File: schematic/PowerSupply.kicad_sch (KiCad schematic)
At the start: 0 parts

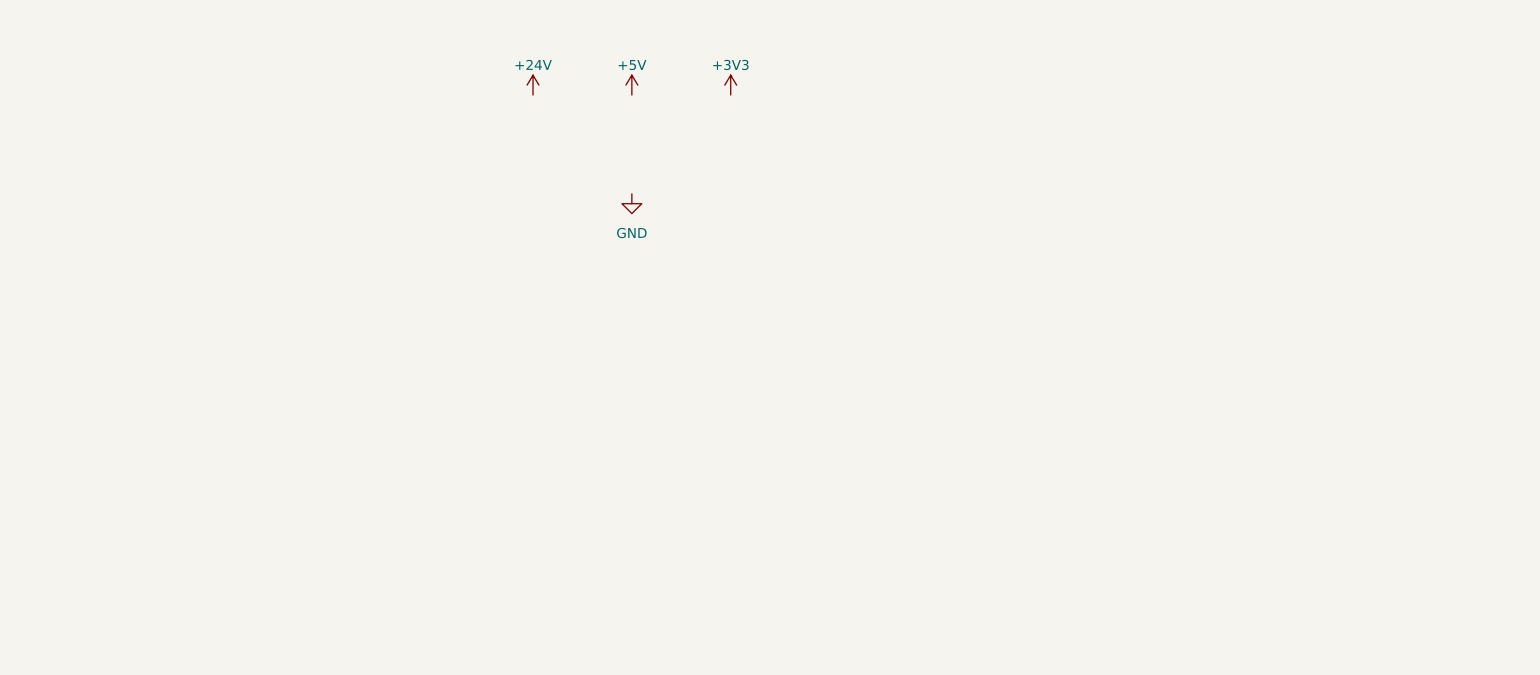
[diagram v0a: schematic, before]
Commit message: Create power supply schematic
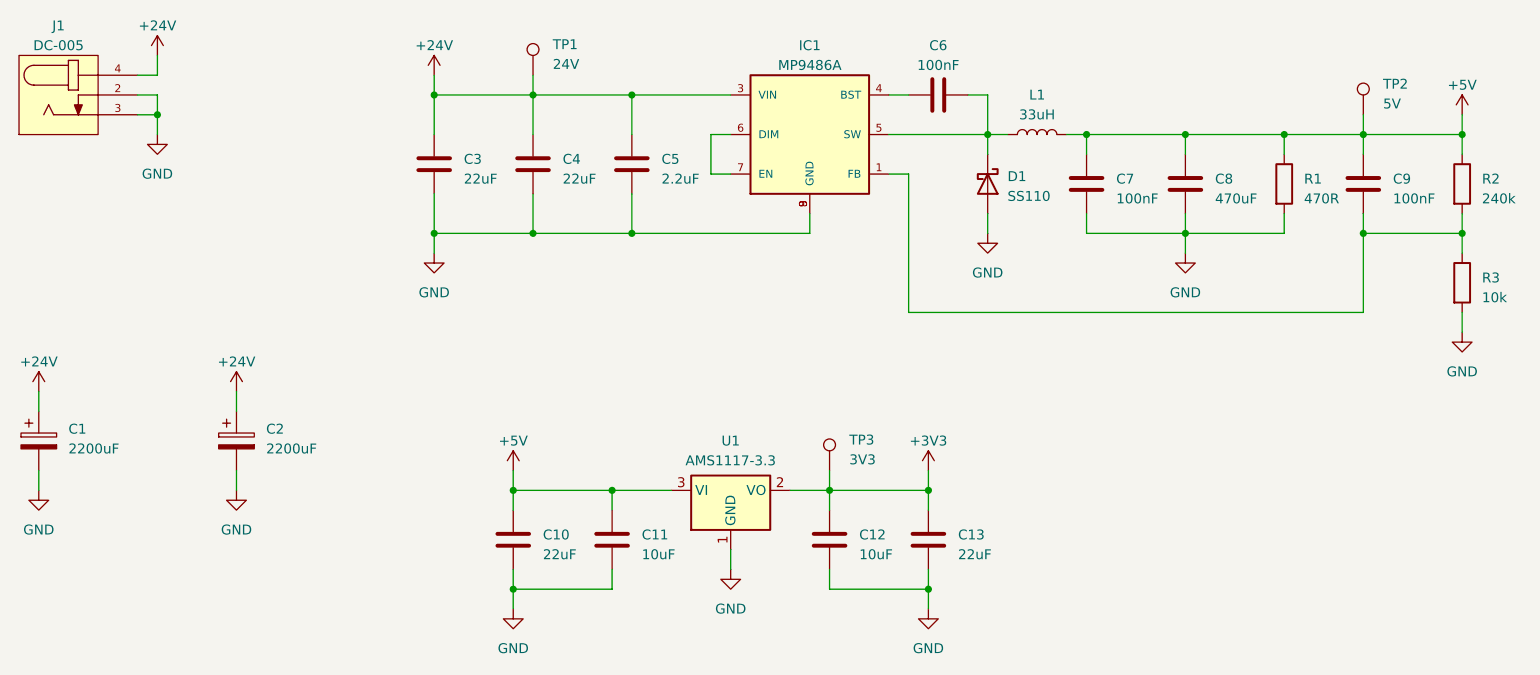
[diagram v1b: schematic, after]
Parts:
- added C1, C2: 2200uF, symbol Device:C_Polarized
- added C10, C13, C3, C4: 22uF, symbol Device:C
- added C11, C12: 10uF, symbol Device:C
- added C5: 2.2uF, symbol Device:C
- added C6, C7, C9: 100nF, symbol Device:C
- added C8: 470uF, symbol Device:C
- added D1: SS110, symbol Device:D_Schottky
- added IC1: MP9486A, MP9486A:SOIC-8EP, symbol MP9486A:MP9486A
- added J1: DC-005, DC-005:NINIGI_DC-005, symbol DC-005:DC-005
- added L1: 33uH, symbol Device:L
- added R1: 470R, symbol Device:R
- added R2: 240k, symbol Device:R
- added R3: 10k, symbol Device:R
- added TP1: 24V, symbol Connector:TestPoint
- added TP2: 5V, symbol Connector:TestPoint
- added TP3: 3V3, symbol Connector:TestPoint
- added U1: AMS1117-3.3, Package_TO_SOT_SMD:SOT-223-3_TabPin2, symbol Regulator_Linear:AMS1117-3.3
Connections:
- net +24V: now also C1.1, C2.1, C3.1, C4.1, C5.1, IC1.3 (VIN), J1.4, TP1.1
- net +3V3: now also C12.1, C13.1, TP3.1, U1.2 (VO)
- net +5V: now also C10.1, C11.1, C7.1, C8.1, C9.1, L1.2, R1.1, R2.1, TP2.1, U1.3 (VI)
- net GND: now also C1.2, C10.2, C11.2, C12.2, C13.2, C2.2, C3.2, C4.2, C5.2, C7.2, C8.2, D1.2 (A), IC1.8 (GND), IC1.9 (GND), J1.2, J1.3, R1.2, R3.2, U1.1 (GND)
- new net: C6.2, D1.1 (K), IC1.5 (SW), L1.1
- new net: C9.2, IC1.1 (FB), R2.2, R3.1
- new net: C6.1, IC1.4 (BST)
- new net: IC1.6 (DIM), IC1.7 (EN)

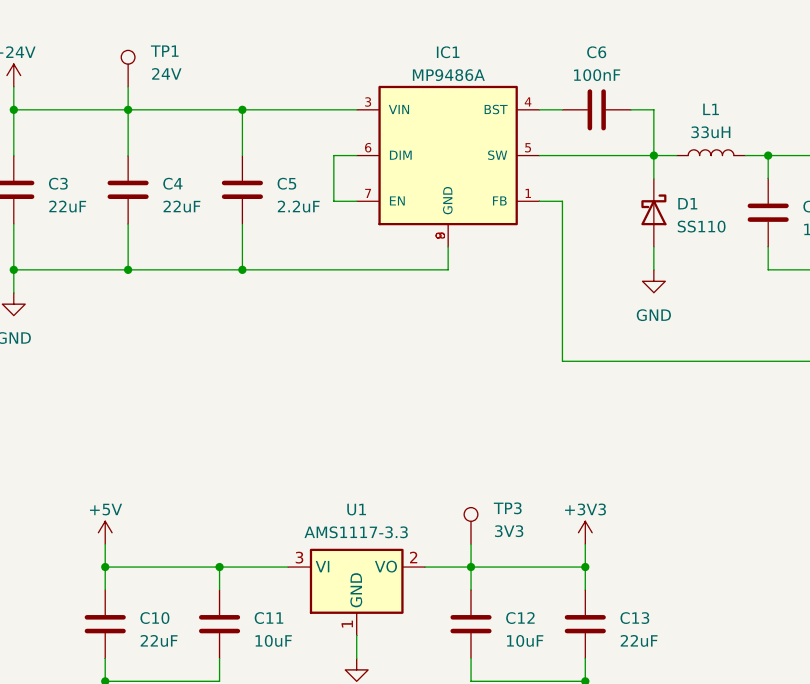
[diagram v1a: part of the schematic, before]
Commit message: Add test points to driver signals
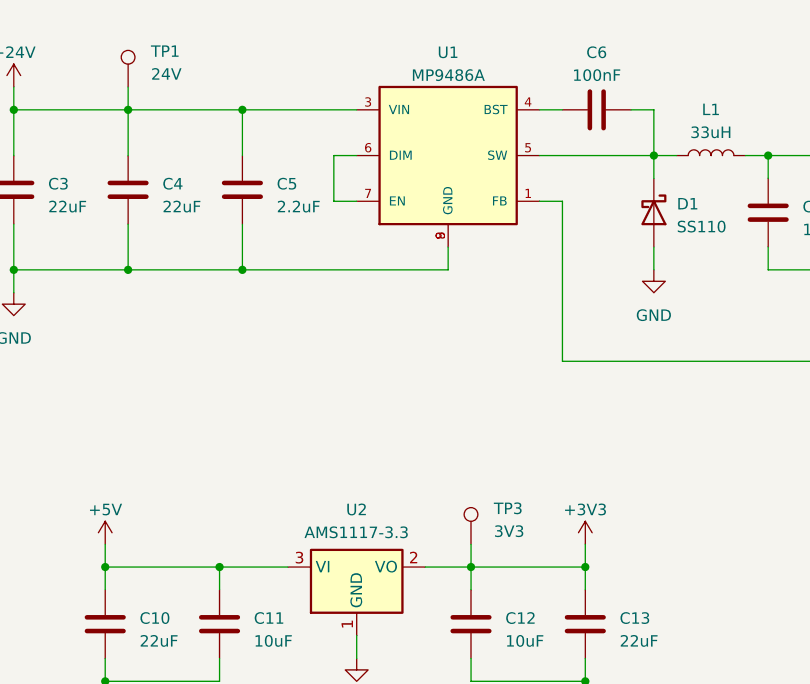
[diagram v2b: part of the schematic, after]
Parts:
- renumbered IC1 to U1, U1 to U2
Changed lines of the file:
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@@
   (symbol (lib_id "Regulator_Linear:AMS1117-3.3") (at 152.4 127 0) (unit 1)
     (in_bom yes) (on_board yes) (dnp no) (fields_autoplaced)
-    (property "Reference" "U1" (at 152.4 120.65 0)
+    (property "Reference" "U2" (at 152.4 120.65 0)
       (effects (font (size 1.27 1.27)))
     )
@@
       (project "uTesla"
         (path "/0cecab2b-a552-4f9c-b012-66fc2b7d8bdb/40e0481b-1d5b-49c7-bf9f-abcc1f3a7809"
-          (reference "U1") (unit 1)
+          (reference "U2") (unit 1)
         )
       )
@@
   (symbol (lib_id "MP9486A:MP9486A") (at 162.56 81.28 0) (unit 1)
     (in_bom yes) (on_board yes) (dnp no) (fields_autoplaced)
-    (property "Reference" "IC1" (at 162.56 69.85 0)
+    (property "Reference" "U1" (at 162.56 69.85 0)
       (effects (font (size 1.27 1.27)))
     )
@@
       (project "uTesla"
         (path "/0cecab2b-a552-4f9c-b012-66fc2b7d8bdb/40e0481b-1d5b-49c7-bf9f-abcc1f3a7809"
-          (reference "IC1") (unit 1)
-        )
-      )
+          (reference "U1") (unit 1)
+        )
+      )

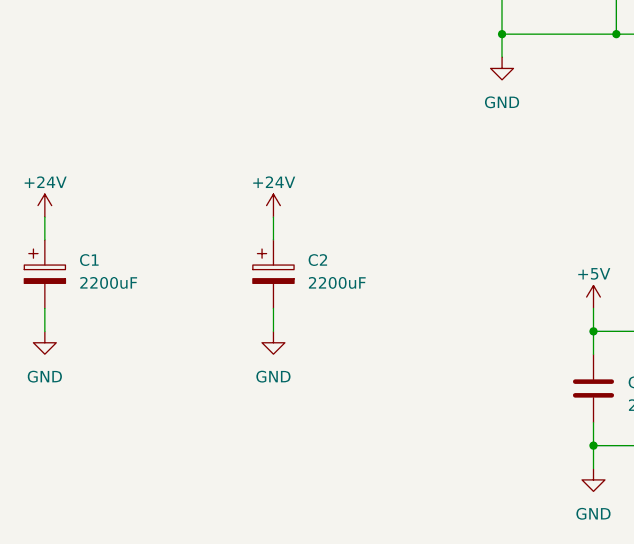
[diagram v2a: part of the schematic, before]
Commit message: Decrease input decoupling capacitance
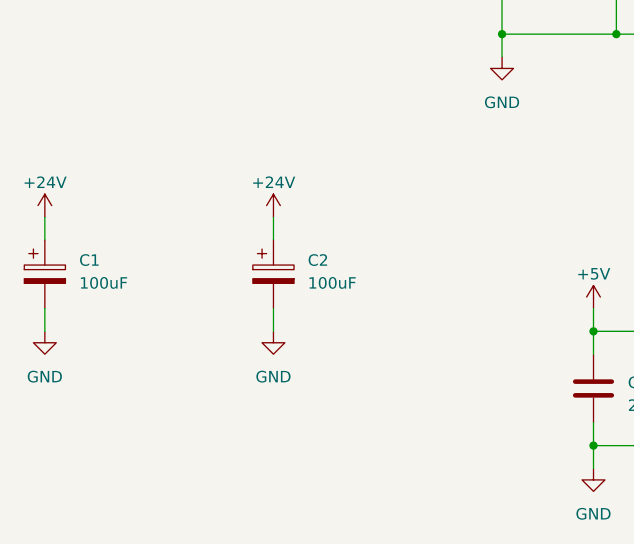
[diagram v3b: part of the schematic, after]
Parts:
- C1, C2: value 2200uF -> 100uF
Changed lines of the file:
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@@
       (effects (font (size 1.27 1.27)) (justify left))
     )
-    (property "Value" "2200uF" (at 92.71 121.666 0)
+    (property "Value" "100uF" (at 92.71 121.666 0)
       (effects (font (size 1.27 1.27)) (justify left))
     )
@@
       (effects (font (size 1.27 1.27)) (justify left))
     )
-    (property "Value" "2200uF" (at 67.31 121.666 0)
-      (effects (font (size 1.27 1.27)) (justify left))
-    )
+    (property "Value" "100uF" (at 67.31 121.666 0)
+      (effects (font (size 1.27 1.27)) (justify left))
+    )

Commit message: Assign footprints
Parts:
- C1, C2: footprint (none) -> Capacitor_THT:CP_Radial_D8.0mm_P3.80mm
- C10, C11, C12, C13, C3, C4, C5, C6, C7, C8, C9: footprint (none) -> Capacitor_SMD:C_0603_1608Metric
- D1: footprint (none) -> Diode_SMD:D_SMA
- L1: footprint (none) -> Inductor_THT:L_Toroid_Vertical_L26.7mm_W14.0mm_P10.16mm_Pulse_D
- R1, R2, R3: footprint (none) -> Resistor_SMD:R_0603_1608Metric
- TP1, TP2, TP3: footprint (none) -> TestPoint:TestPoint_Pad_D2.0mm
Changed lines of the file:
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@@
       (effects (font (size 1.27 1.27)) (justify left))
     )
-    (property "Footprint" "" (at 185.42 87.63 0)
+    (property "Footprint" "Diode_SMD:D_SMA" (at 185.42 87.63 0)
       (effects (font (size 1.27 1.27)) hide)
     )
@@
       (effects (font (size 1.27 1.27)) (justify left))
     )
-    (property "Footprint" "" (at 199.0852 91.44 0)
+    (property "Footprint" "Capacitor_SMD:C_0603_1608Metric" (at 199.0852 91.44 0)
       (effects (font (size 1.27 1.27)) hide)
     )
@@
       (effects (font (size 1.27 1.27)) (justify left))
     )
-    (property "Footprint" "" (at 127.9652 88.9 0)
+    (property "Footprint" "Capacitor_SMD:C_0603_1608Metric" (at 127.9652 88.9 0)
       (effects (font (size 1.27 1.27)) hide)
     )
@@
       (effects (font (size 1.27 1.27)) (justify left))
     )
-    (property "Footprint" "" (at 244.602 100.33 90)
+    (property "Footprint" "Resistor_SMD:R_0603_1608Metric" (at 244.602 100.33 90)
       (effects (font (size 1.27 1.27)) hide)
     )
@@
       (effects (font (size 1.27 1.27)) (justify left))
     )
-    (property "Footprint" "" (at 138.1252 137.16 0)
+    (property "Footprint" "Capacitor_SMD:C_0603_1608Metric" (at 138.1252 137.16 0)
       (effects (font (size 1.27 1.27)) hide)
     )
@@
       (effects (font (size 1.27 1.27)) (justify left))
     )
-    (property "Footprint" "" (at 166.0652 137.16 0)
+    (property "Footprint" "Capacitor_SMD:C_0603_1608Metric" (at 166.0652 137.16 0)
       (effects (font (size 1.27 1.27)) hide)
     )
@@
       (effects (font (size 1.27 1.27)) (justify left))
     )
-    (property "Footprint" "" (at 178.7652 137.16 0)
+    (property "Footprint" "Capacitor_SMD:C_0603_1608Metric" (at 178.7652 137.16 0)
       (effects (font (size 1.27 1.27)) hide)
     )
@@
       (effects (font (size 1.27 1.27)) (justify left))
     )
-    (property "Footprint" "" (at 89.8652 124.46 0)
+    (property "Footprint" "Capacitor_THT:CP_Radial_D8.0mm_P3.80mm" (at 89.8652 124.46 0)
       (effects (font (size 1.27 1.27)) hide)
     )
@@
       (effects (font (size 1.27 1.27)) (justify left))
     )
-    (property "Footprint" "" (at 238.76 78.74 0)
+    (property "Footprint" "TestPoint:TestPoint_Pad_D2.0mm" (at 238.76 78.74 0)
       (effects (font (size 1.27 1.27)) hide)
     )
@@
       (effects (font (size 1.27 1.27)) (justify left))
     )
-    (property "Footprint" "" (at 244.602 87.63 90)
+    (property "Footprint" "Resistor_SMD:R_0603_1608Metric" (at 244.602 87.63 90)
       (effects (font (size 1.27 1.27)) hide)
     )
@@
       (effects (font (size 1.27 1.27)) (justify left))
     )
-    (property "Footprint" "" (at 211.7852 91.44 0)
+    (property "Footprint" "Capacitor_SMD:C_0603_1608Metric" (at 211.7852 91.44 0)
       (effects (font (size 1.27 1.27)) hide)
     )
@@
       (effects (font (size 1.27 1.27)) (justify left))
     )
-    (property "Footprint" "" (at 140.6652 88.9 0)
+    (property "Footprint" "Capacitor_SMD:C_0603_1608Metric" (at 140.6652 88.9 0)
       (effects (font (size 1.27 1.27)) hide)
     )
@@
       (effects (font (size 1.27 1.27)) (justify left))
     )
-    (property "Footprint" "" (at 132.08 73.66 0)
+    (property "Footprint" "TestPoint:TestPoint_Pad_D2.0mm" (at 132.08 73.66 0)
       (effects (font (size 1.27 1.27)) hide)
     )
@@
       (effects (font (size 1.27 1.27)))
     )
-    (property "Footprint" "" (at 182.88 75.2348 0)
+    (property "Footprint" "Capacitor_SMD:C_0603_1608Metric" (at 182.88 75.2348 0)
       (effects (font (size 1.27 1.27)) hide)
     )
@@
       (effects (font (size 1.27 1.27)) (justify left))
     )
-    (property "Footprint" "" (at 221.742 87.63 90)
+    (property "Footprint" "Resistor_SMD:R_0603_1608Metric" (at 221.742 87.63 90)
       (effects (font (size 1.27 1.27)) hide)
     )
@@
       (effects (font (size 1.27 1.27)) (justify left))
     )
-    (property "Footprint" "" (at 170.18 124.46 0)
+    (property "Footprint" "TestPoint:TestPoint_Pad_D2.0mm" (at 170.18 124.46 0)
       (effects (font (size 1.27 1.27)) hide)
     )
@@
       (effects (font (size 1.27 1.27)) (justify left))
     )
-    (property "Footprint" "" (at 125.4252 137.16 0)
+    (property "Footprint" "Capacitor_SMD:C_0603_1608Metric" (at 125.4252 137.16 0)
       (effects (font (size 1.27 1.27)) hide)
     )
@@
       (effects (font (size 1.27 1.27)) (justify left))
     )
-    (property "Footprint" "" (at 234.6452 91.44 0)
+    (property "Footprint" "Capacitor_SMD:C_0603_1608Metric" (at 234.6452 91.44 0)
       (effects (font (size 1.27 1.27)) hide)
     )
@@
       (effects (font (size 1.27 1.27)) (justify left))
     )
-    (property "Footprint" "" (at 115.2652 88.9 0)
+    (property "Footprint" "Capacitor_SMD:C_0603_1608Metric" (at 115.2652 88.9 0)
       (effects (font (size 1.27 1.27)) hide)
     )
@@
       (effects (font (size 1.27 1.27)) (justify left))
     )
-    (property "Footprint" "" (at 64.4652 124.46 0)
+    (property "Footprint" "Capacitor_THT:CP_Radial_D8.0mm_P3.80mm" (at 64.4652 124.46 0)
       (effects (font (size 1.27 1.27)) hide)
     )
@@
       (effects (font (size 1.27 1.27)))
     )
-    (property "Footprint" "" (at 191.77 81.28 0)
-      (effects (font (size 1.27 1.27)) hide)
-    )
+    (property "Footprint" "Inductor_THT:L_Toroid_Vertical_L26.7mm_W14.0mm_P10.16mm_Pulse_D" (at 191.77 81.28 0)
+      (effects (font (size 1.27 1.27)) hide)
+    )

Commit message: Add power switch
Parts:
- added J19: ~, Custom:SolderPad-3pin, symbol Custom:SolderPad-3pin
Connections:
- net +24V: now also J19.2; no longer J1.4
- net GND: now also J19.3
- new net: J1.4, J19.1
